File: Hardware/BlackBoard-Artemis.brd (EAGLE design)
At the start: 68.6 x 53.3 mm, 93 parts, among them IC3 LM1117, J2 CORTEX_DEBUG, J3 POWER_JACKTOE, J5 USB-C, Q1 1.1A/60V/600mΩ, U2 ARTEMIS_FULL, U3 AP2112-3.3V, U5 CH340C, Y1 32.768kHz

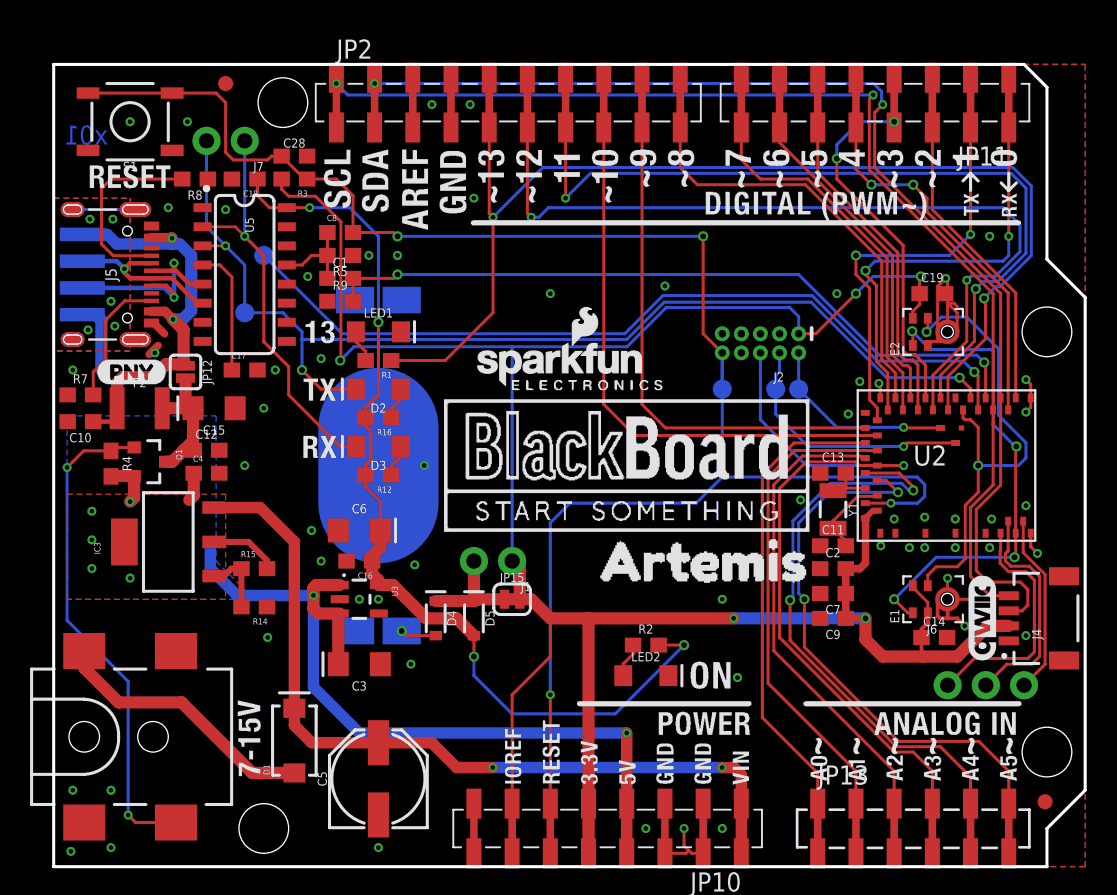
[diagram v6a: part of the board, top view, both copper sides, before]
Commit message: Version x02 - now uses Artemis v10. One mic, more GPIO, better silk,
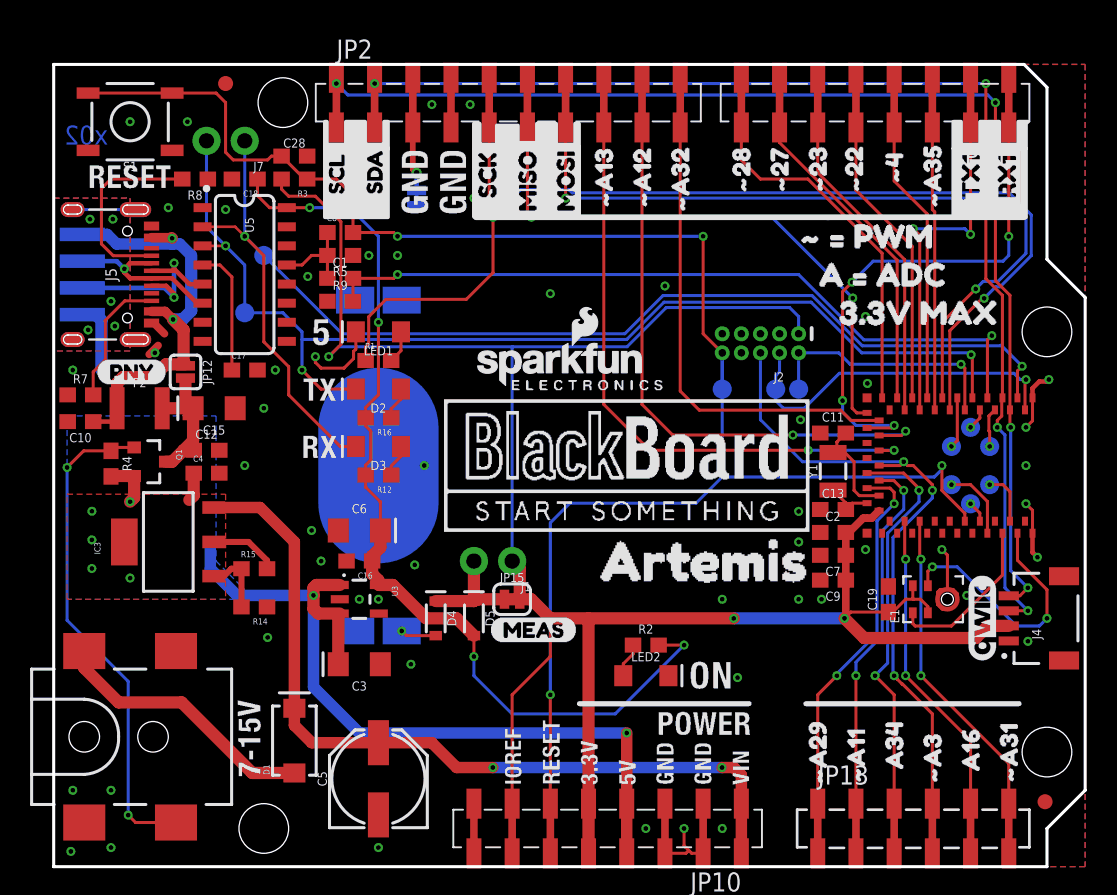
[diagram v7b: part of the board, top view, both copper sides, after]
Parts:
- removed C14: 0.1uF, SparkFun-Capacitors:0603
- removed E2: SPH0641LM4H-1, SparkFun-Sensors:SPH0641LM4H-1_MICROPHONE
- removed J6: (no value), SparkFun-Connectors:1X03_NO_SILK
- removed U$18: (no value), buzzard_labels:RX03
- removed U2: ARTEMIS_FULL, Module-Pads:ARTEMIS
- added JP16: (no value), SparkFun-Jumpers:SMT-JUMPER_2_NC_TRACE_SILK
- added TP11, TP12, TP13, TP14, TP8, TP9: (no value), SparkFun-Connectors:PAD.03X.05
- added U$17: (no value), buzzard_labels:A160
- added U$19: (no value), buzzard_labels (1):#48
- added U$21: (no value), buzzard_labels (1):#229
- added U$25: (no value), buzzard_labels (1):#2310
- added U$26: (no value), buzzard_labels (1):#2711
- added U$27: (no value), buzzard_labels (1):#2812
- added U$28: (no value), buzzard_labels (1):#A31
- added U$29: (no value), buzzard_labels (1):#A113
- added U$30: (no value), buzzard_labels (1):#A294
- added U$31: (no value), buzzard_labels (1):#A310
- added U$33: (no value), buzzard_labels (1):#A357
- added U$34: (no value), buzzard_labels (1):#A1214
- added U$35: (no value), buzzard_labels (1):#A1315
- added U$36: (no value), buzzard_labels (1):#A3213
- added U$38: (no value), buzzard_labels (1):A342
- added U$47: (no value), buzzard_labels (8):MISO8
- added U$48: (no value), buzzard_labels (8):MOSI7
- added U$49: (no value), buzzard_labels (3):RX01
- added U$50: (no value), buzzard_labels (8):SCK9
- added U$53: (no value), buzzard_labels (3):TX00
- added U$57: (no value), buzzard_labels (10):SCL3
- added U$58: (no value), buzzard_labels (10):SDA4
- added U$60: (no value), buzzard_labels (1):#425
- added U$61: (no value), buzzard_labels (1):#434
- added U$62: (no value), buzzard_labels (1):80
- added U$63: (no value), buzzard_labels (1):91
- added U$64: (no value), buzzard_labels (1):102
- added U$65: (no value), buzzard_labels (1):383
- added U$66: (no value), buzzard_labels (2):#_#_PWM7
- added U$67: (no value), buzzard_labels (2):3#3V_MAX2
- added U$69: (no value), buzzard_labels (2):A_#_ADC6
- added U$70: (no value), buzzard_labels (2):MEAS3
- added U$71: (no value), buzzard_labels (2):RX11
- added U$72: (no value), buzzard_labels (2):TX10
- added U4: ARTEMIS_MODULESMD, Testing:ARTEMIS_FP
- U$20: device buzzard_labels:TX02 -> buzzard_labels (5):AREF2
- moved FRAME2 87.1 mm to (36.8, 21.6), flipped to the bottom, turned to 270 degrees
- moved C19 20.5 mm to (55.5, 17.8), turned to 90 degrees
- moved U$20 17.7 mm to (26.9, 46.7), turned to 0 degrees
- moved C11 7.49 mm to (51.8, 28.8)
- moved Y1 2.54 mm to (51.8, 26.3), turned to 90 degrees
- moved C7 2.54 mm to (51.8, 20.7)
- moved C9 2.54 mm to (51.8, 19.1)
- moved C13 2.41 mm to (51.8, 23.7)
- moved C2 2.41 mm to (51.8, 22.2)
- turned LED1 to 180 degrees
- turned R1 to 0 degrees
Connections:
- removed net D11/MOSI: JP2.7A, JP2.7B, U2.12
- removed net D4: JP11.5A, JP11.5B, U2.3
- removed net SDA: J4.3, JP2.2A, JP2.2B, U2.4
- removed net ~AD0: JP13.1A, JP13.1B, U2.25
- removed net ~AD1: JP13.2A, JP13.2B, U2.26
- removed net ~AD2: JP13.3A, JP13.3B, U2.27
- removed net ~AD4: JP13.5A, JP13.5B, U2.29
- removed net ~AD5: JP13.6A, JP13.6B, U2.30
- removed net ~D10: JP2.8A, JP2.8B, U2.24
- removed net ~D12/MISO: JP2.6A, JP2.6B, U2.13
- removed net ~D13/SCK: JP2.5A, JP2.5B, R1.1, U2.11
- removed net ~D14: J6.1, U2.41
- removed net ~D15: J6.2, U2.42
- removed net ~D16: J6.3, U2.44
- removed net ~D2: JP11.3A, JP11.3B, U2.2
- removed net ~D3: JP11.4A, JP11.4B, U2.14
- removed net ~D5: JP11.6A, JP11.6B, U2.15
- removed net ~D6: JP11.7A, JP11.7B, U2.16
- removed net ~D7: JP11.8A, JP11.8B, U2.17
- removed net ~D8: JP2.10A, JP2.10B, U2.18
- removed net ~D9: JP2.9A, JP2.9B, U2.23
- removed net ~RXI-1: JP11.1A, JP11.1B, U2.19
- removed net ~SCL: J4.4, JP2.1A, JP2.1B, U2.5
- removed net ~TXO-1: JP11.2A, JP11.2B, U2.22
- new net AD16: JP13.5A, JP13.5B, U4.AD16
- new net AD34: JP13.3A, JP13.3B, U4.AD34
- new net D10: TP14.P$1, U4.D10
- new net D38: TP11.P$1, U4.D38
- new net D40/SDA: J4.3, JP2.2A, JP2.2B, U4.D40
- new net D7/MOSI: JP2.7A, JP2.7B, U4.D7
- new net D8: TP12.P$1, U4.D8
- new net D9: TP13.P$1, U4.D9
- new net N$10: JP16.2, JP2.3A, JP2.3B
- new net ~AD11: JP13.2A, JP13.2B, U4.~AD11
- new net ~AD12: JP2.9A, JP2.9B, U4.~AD12
- new net ~AD13: JP2.8A, JP2.8B, U4.~AD13
- new net ~AD29: JP13.1A, JP13.1B, U4.~AD29
- new net ~AD31: JP13.6A, JP13.6B, U4.~AD31
- new net ~AD32: JP2.10A, JP2.10B, U4.~AD32
- new net ~AD35: JP11.3A, JP11.3B, U4.~AD35
- new net ~D22: JP11.5A, JP11.5B, U4.~D22
- new net ~D23: JP11.6A, JP11.6B, U4.~D23
- new net ~D24/TXO-1: JP11.2A, JP11.2B, U4.~D24
- new net ~D25/RXI-1: JP11.1A, JP11.1B, U4.~D25
- new net ~D27: JP11.7A, JP11.7B, U4.~D27
- new net ~D28: JP11.8A, JP11.8B, U4.~D28
- new net ~D39/SCL: J4.4, JP2.1A, JP2.1B, U4.~D39
- new net ~D4: JP11.4A, JP11.4B, U4.~D4
- new net ~D42: TP9.P$1, U4.~D42
- new net ~D43: TP8.P$1, U4.~D43
- new net ~D5/SCK: JP2.5A, JP2.5B, R1.1, U4.~D5
- new net ~D6/MISO: JP2.6A, JP2.6B, U4.~D6
- net !RESET: now also U4.~RST; no longer U2.33
- net BOOT: now also U4.BOOT; no longer U2.6
- net GND: now also JP16.1, U4.GND@1, U4.GND@22, U4.GND@38, U4.GND@39, U4.GND@47, U4.GND@59; no longer C14.2, E2.2, E2.3, E2.6, E2.7, E2.8, U2.1, U2.20, U2.21, U2.36, U2.37, U2.38, U2.39, U2.40, U2.45
- net N$7: now also U4.XO; no longer U2.32
- net N$8: now also U4.XI; no longer U2.31
- net PDMCLK: now also U4.~D37; no longer E2.4, U2.9
- net PDMDATA: now also U4.D36; no longer E2.1, U2.43
- net RXI-0: now also U4.RXI-0; no longer U2.7
- net SWDCK: now also U4.SWDCK; no longer U2.47
- net SWDIO: now also U4.SWDIO; no longer U2.46
- net TXO-0: now also U4.TXO-0; no longer U2.8
- net VDD: now also U4.VDD@36, U4.VDD@37; no longer C14.1, E2.5, U2.34, U2.35
- net ~AD3/SWO: now also U4.~AD33/SWO; no longer U2.28
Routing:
- net ~D39/SCL: track 0.00 -> 82.3 mm, vias 0 -> 4
- net D40/SDA: track 0.00 -> 81.7 mm, vias 0 -> 4
- net SDA: track 79.9 -> 0.00 mm, vias 2 -> 0
- net ~D13/SCK: track 78.9 -> 0.00 mm, vias 2 -> 0
- net ~SCL: track 78.5 -> 0.00 mm, vias 2 -> 0
- net ~D5/SCK: track 0.00 -> 78.2 mm, vias 0 -> 2
- net ~D12/MISO: track 58.3 -> 0.00 mm, vias 2 -> 0
- net D11/MOSI: track 56.6 -> 0.00 mm, vias 2 -> 0
- net D7/MOSI: track 0.00 -> 54.0 mm, vias 0 -> 2
- net ~AD13: track 0.00 -> 43.3 mm, vias 0 -> 2
- net ~AD12: track 0.00 -> 42.1 mm, vias 0 -> 2
- net ~AD4: track 41.9 -> 0.00 mm, vias 2 -> 0
- net ~D6/MISO: track 0.00 -> 41.4 mm, vias 0 -> 2
- net ~D10: track 40.8 -> 0.00 mm
- net ~AD5: track 40.0 -> 0.00 mm, vias 2 -> 0
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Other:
- board text added: "x02"
- board text removed: "x01"

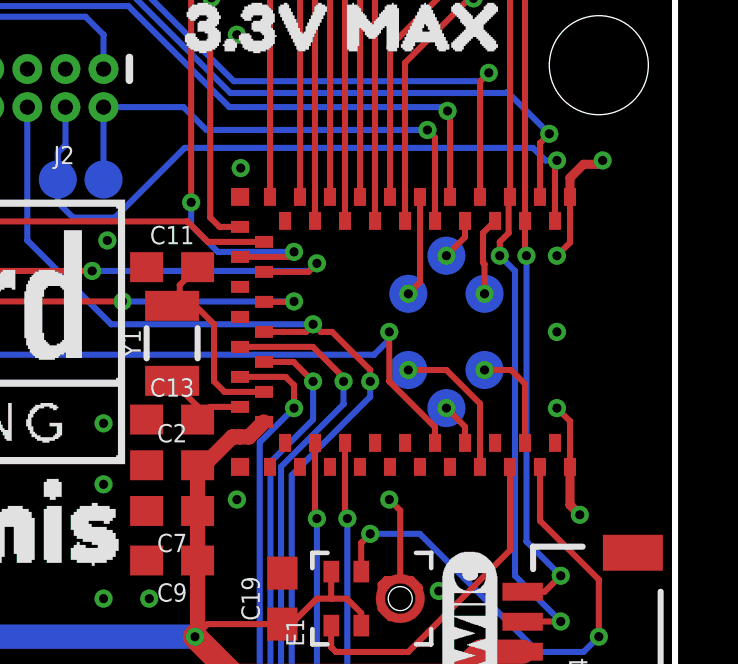
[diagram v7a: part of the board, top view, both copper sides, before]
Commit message: Update silk on Artemis FP
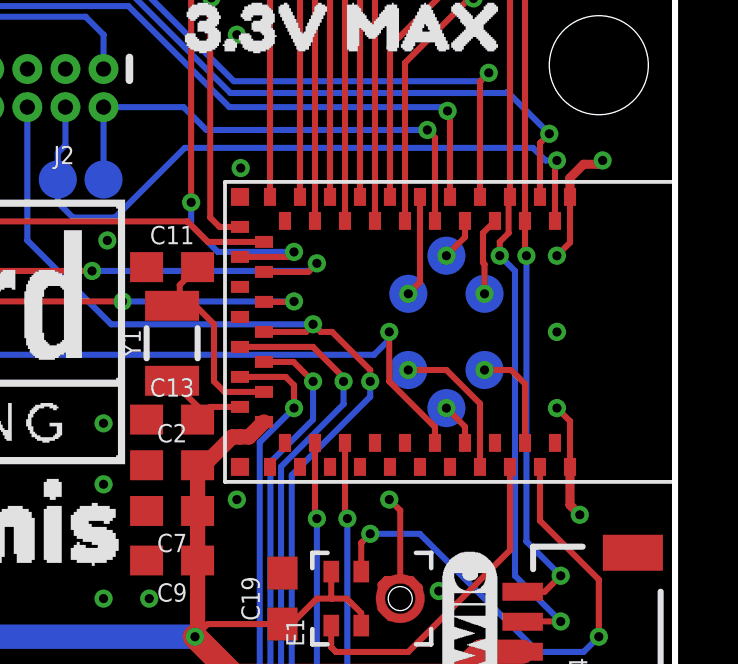
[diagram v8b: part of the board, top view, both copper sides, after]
